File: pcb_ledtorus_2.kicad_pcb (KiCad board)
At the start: 4 copper layers, 199 x 199 mm, 273 parts, among them P1 CONN_02X04, P2 CONN_6, P3 MICRO-SD, P4 CONN_2, P5 KNUSB, P6 CONN_12, U1 STM32F46X_LQFP176, U10 TLC5955, U11 TLC5955, U12 TLC5955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

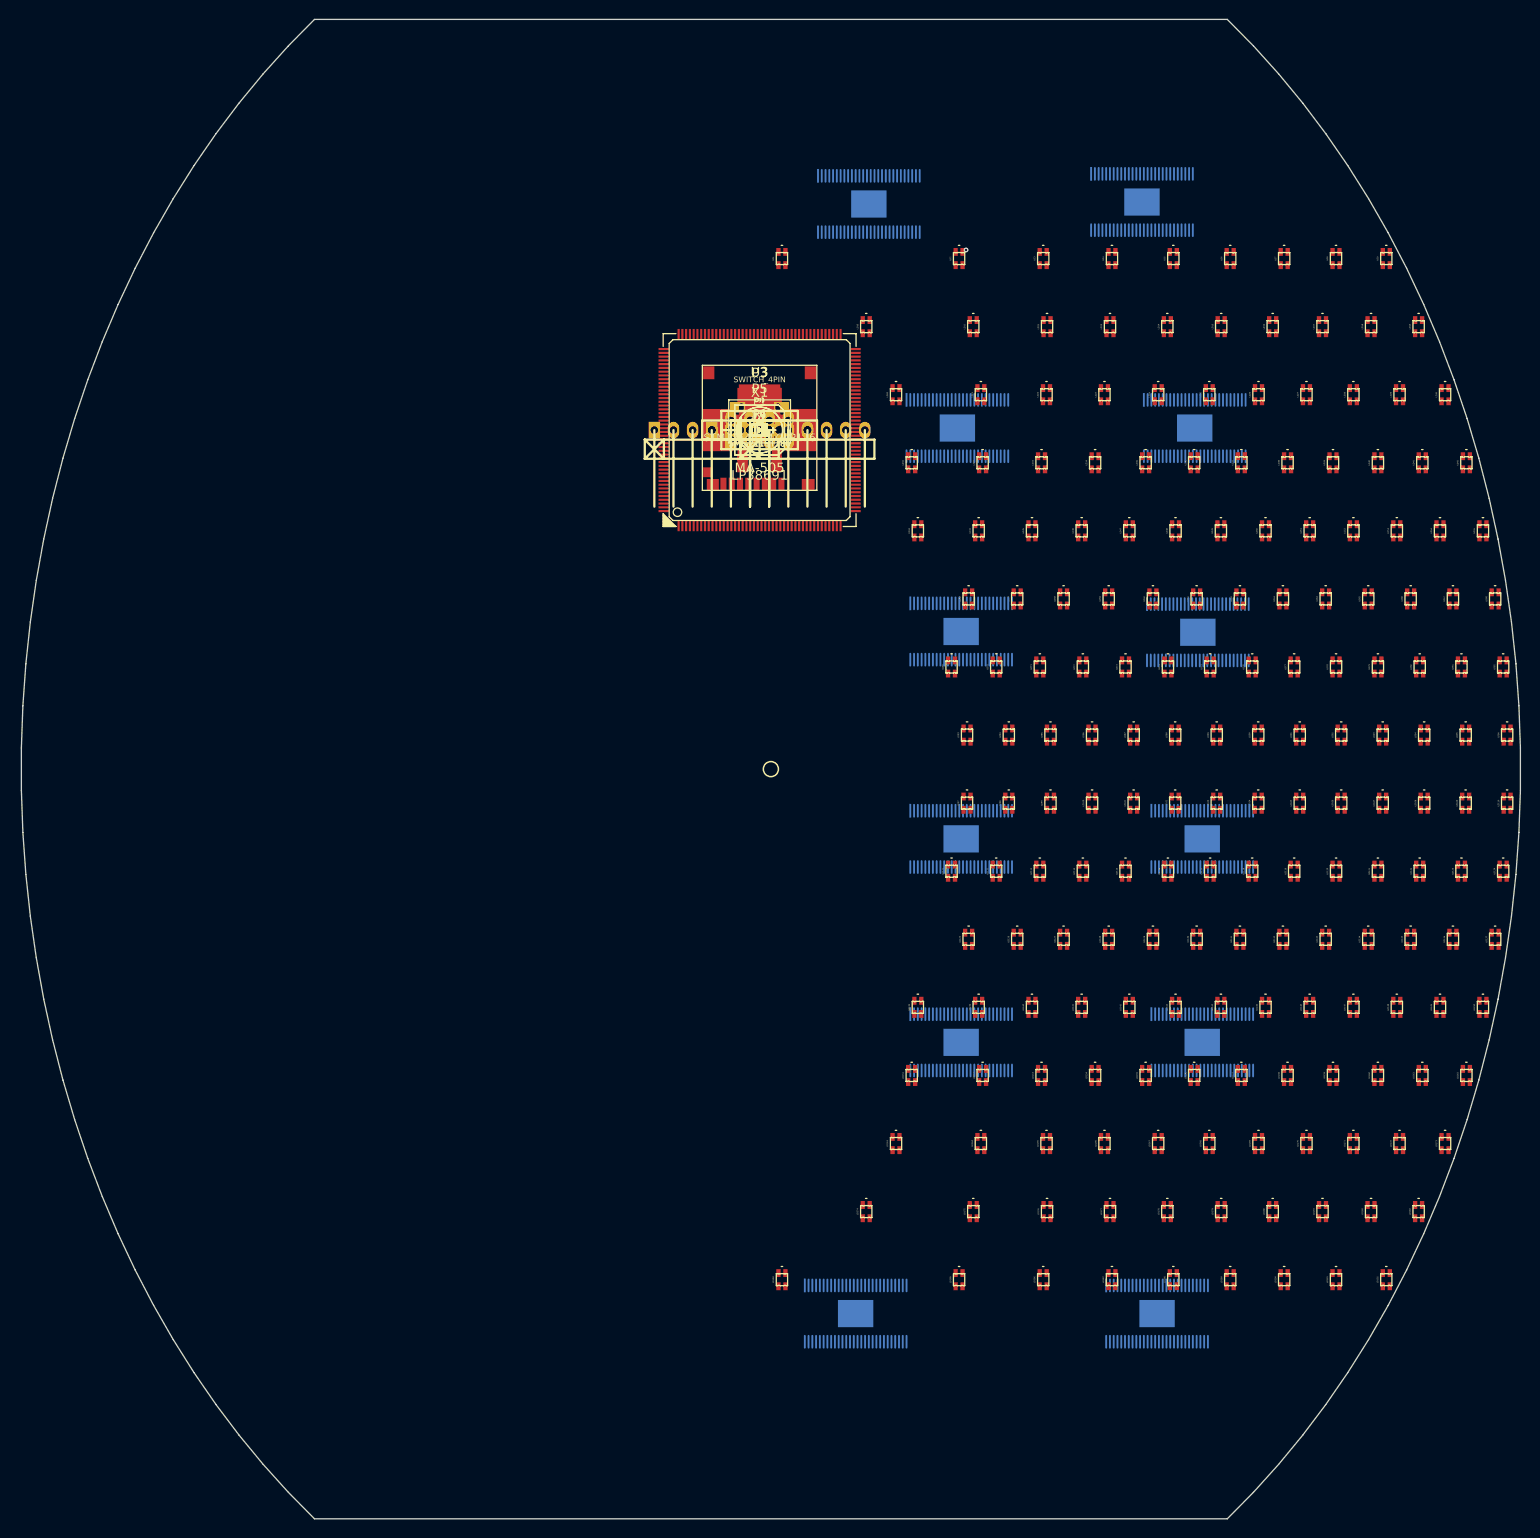
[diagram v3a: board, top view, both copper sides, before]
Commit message: Move a couple footprints out a bit.
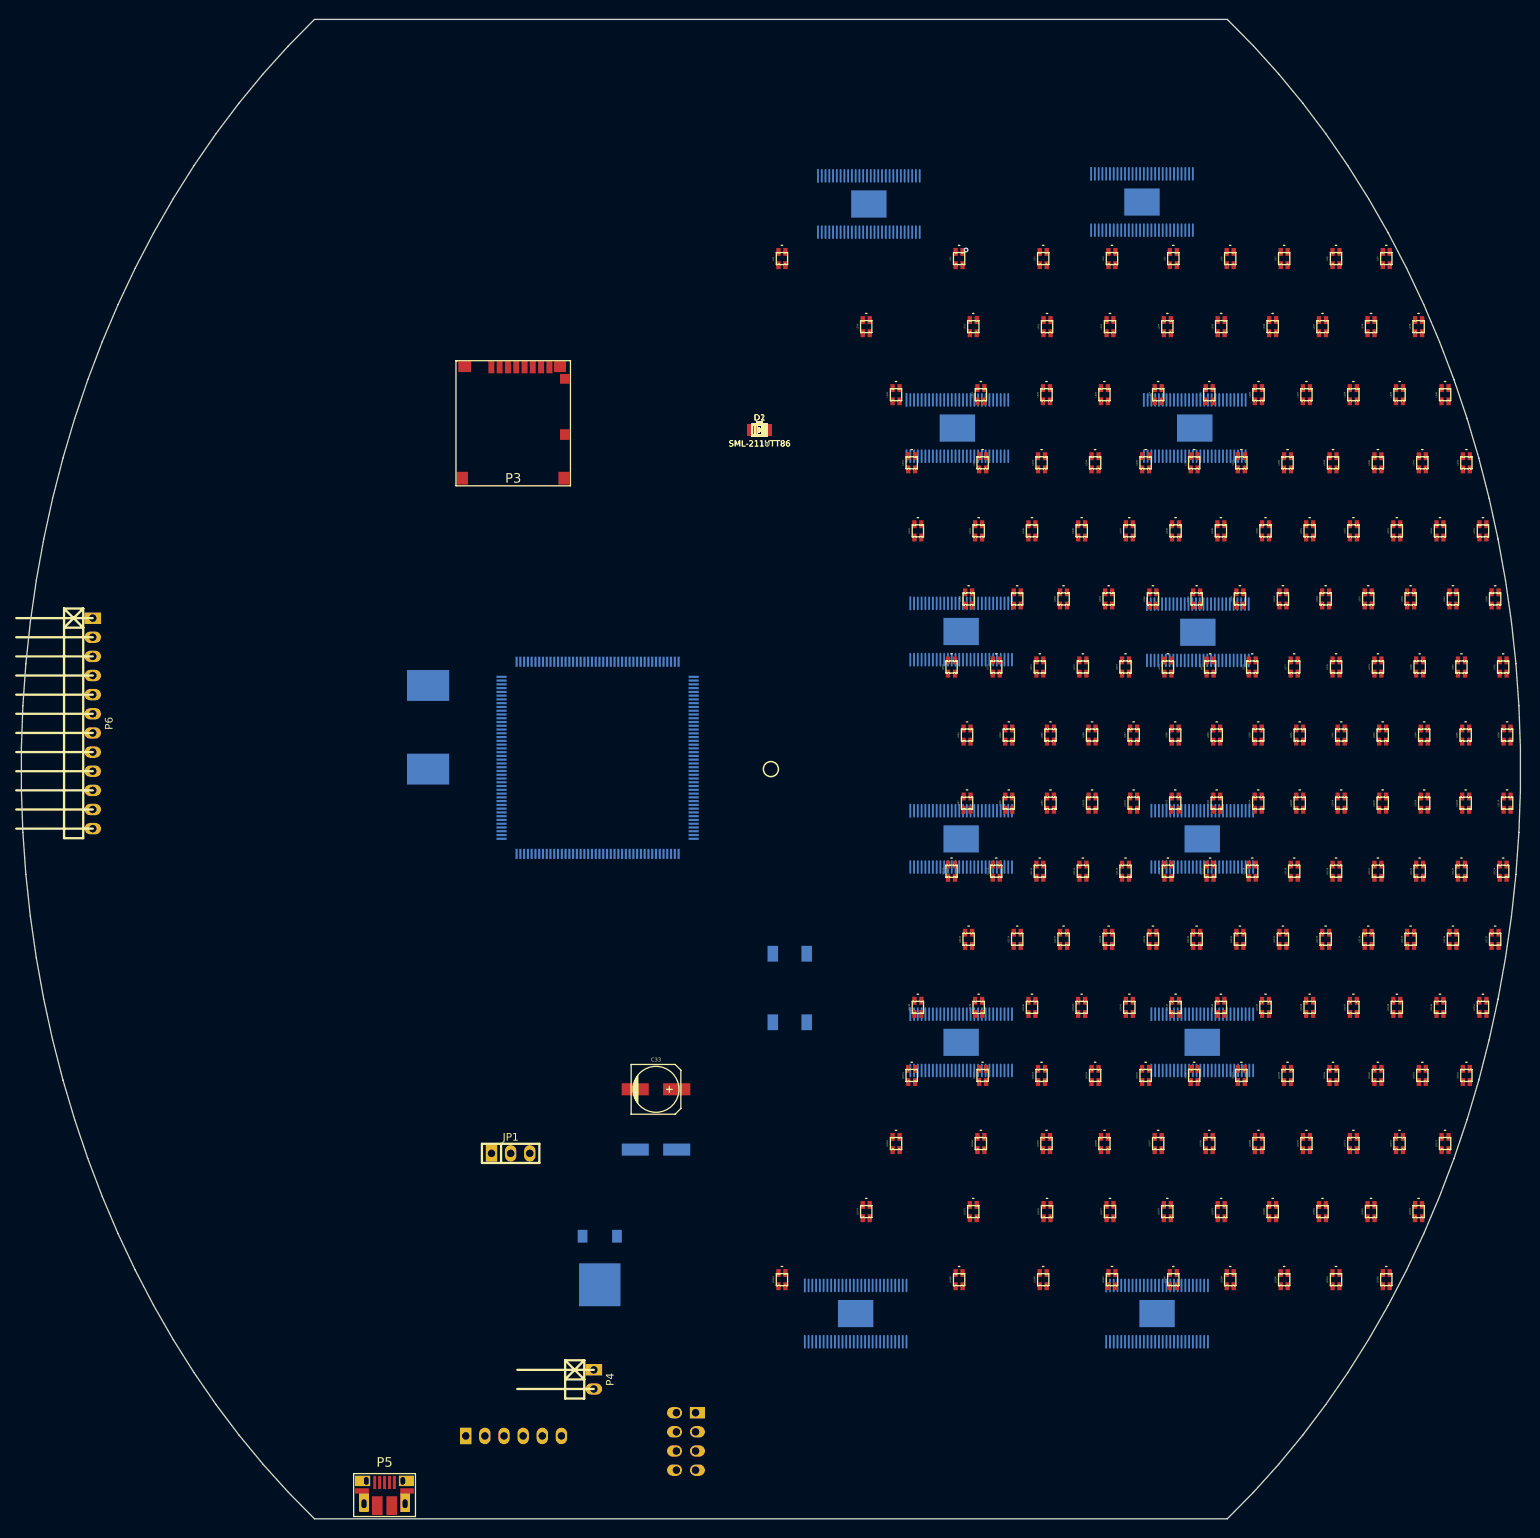
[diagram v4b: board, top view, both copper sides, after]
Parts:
- B1, C32, P1, P2, U1, U3, X1: moved to B.Cu
- moved P5 150.9 mm to (98.7, 247.5)
- moved P2 137.4 mm to (115.8, 238.5)
- moved P1 134.6 mm to (138.7, 239.2), turned to 270 degrees
- moved P4 127.9 mm to (126.5, 231.0), turned to 270 degrees
- moved U3 112.2 mm to (127.3, 215.2)
- moved JP1 101.5 mm to (115.5, 201.0)
- moved P6 96.7 mm to (60.0, 143.9), turned to 270 degrees
- moved C32 96.5 mm to (134.8, 200.5)
- moved C33 88.6 mm to (134.8, 192.5)
- moved B1 74.2 mm to (152.5, 179.0)
- moved X1 59.1 mm to (104.5, 144.5), turned to 90 degrees
- moved U1 48.5 mm to (127.0, 148.5), turned to 90 degrees
- moved P3 32.7 mm to (115.8, 103.8), turned to 180 degrees

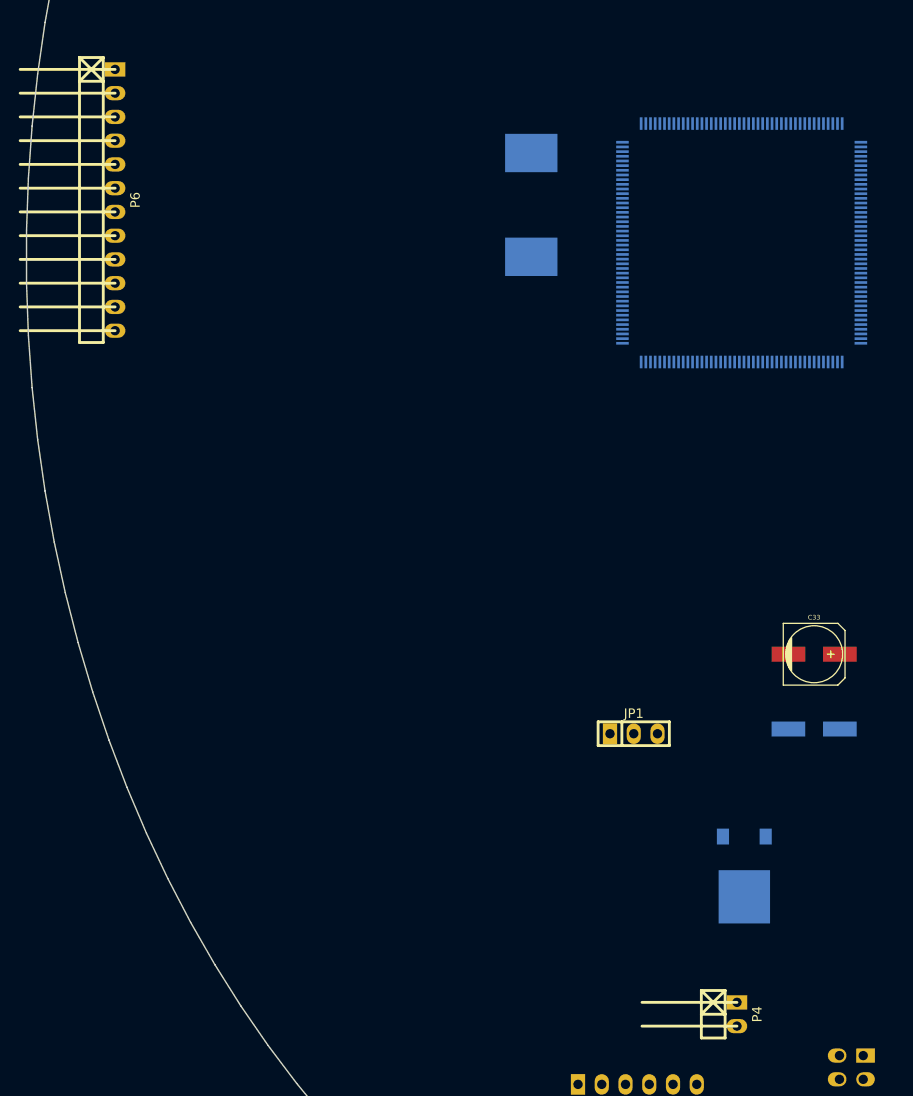
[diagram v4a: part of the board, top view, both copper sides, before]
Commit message: Component PCB sides, and 3d models.
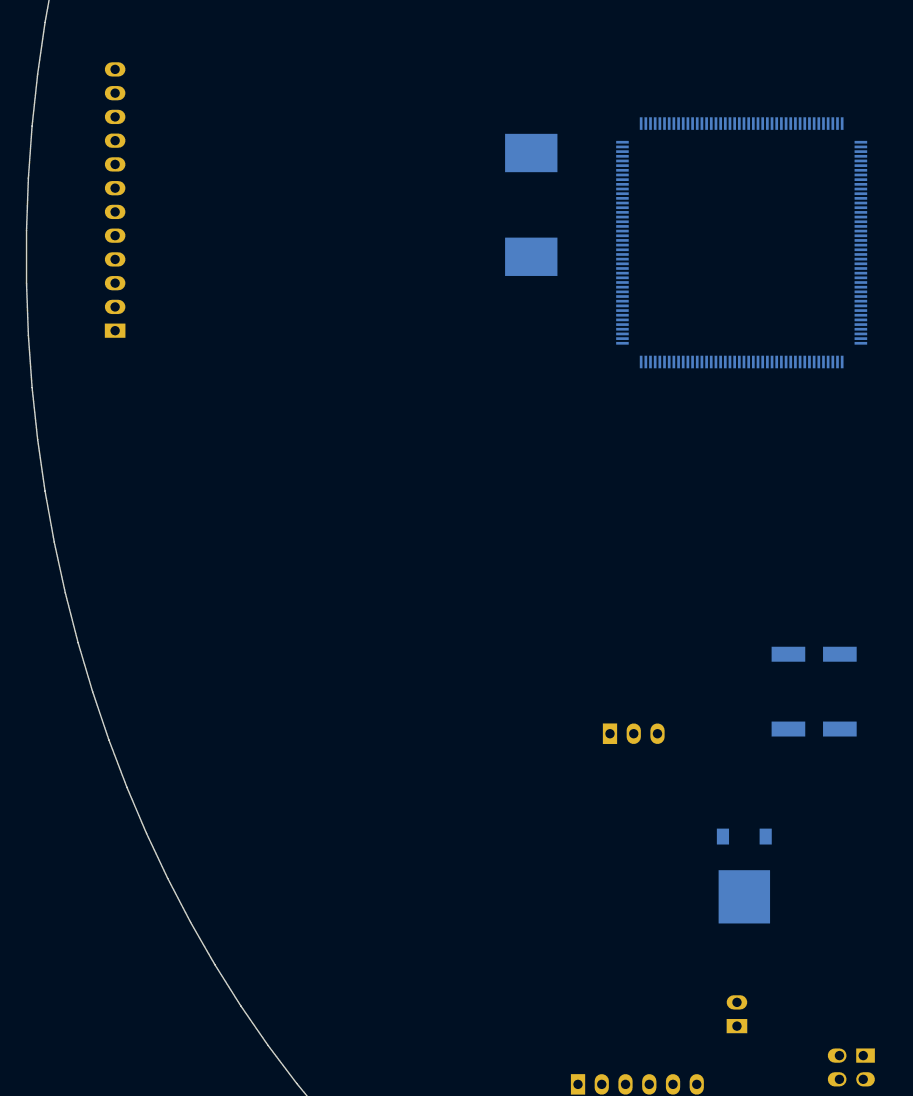
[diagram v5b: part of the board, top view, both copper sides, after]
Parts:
- C33, JP1, P4, P6: moved to B.Cu
- turned P4 to 90 degrees
- turned P6 to 90 degrees
